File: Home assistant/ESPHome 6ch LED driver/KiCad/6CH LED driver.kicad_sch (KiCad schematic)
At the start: 75 parts, among them J1 DC Power, J10 I2C ext, J11 UART int, J12 UART ext, J13 IO Out, J14 U Out, J2 USB_C_small, J3 LED 1, J4 LED 2, J5 LED 3, J6 LED 4, J7 LED 5, J8 LED 6, J9 I2C int, Q1 AP4409AGEM, Q2 AP4409AGEM, Q3 AO3400A, Q4 AO3400A, Q5 AO3400A, Q6 AO3400A, Q7 AO3400A, Q8 AO3400A, SW1 Reset, SW2 Boot, U1 TPS5430DDA, U2 AMS1117-3.3, U3 ESP32-C6-WROOM-1

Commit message: Fix USB
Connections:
- net USB D+: now also R4.1; no longer R5.1
- net USB D-: now also R5.1; no longer R4.1
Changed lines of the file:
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@@
-    )
-  )
-  (global_label "USB D+" (shape bidirectional) (at 114.3 36.83 0) (fields_autoplaced)
-    (effects (font (size 1 1)) (justify left))
-    (property "Intersheetrefs" "${INTERSHEET_REFS}" (at 123.5253 36.83 0)
-      (effects (font (size 1.27 1.27)) (justify left) hide)
     )
   )
@@
     )
   )
+  (global_label "USB D+" (shape bidirectional) (at 114.3 31.75 0) (fields_autoplaced)
+    (effects (font (size 1 1)) (justify left))
+    (property "Intersheetrefs" "${INTERSHEET_REFS}" (at 123.5253 31.75 0)
+      (effects (font (size 1.27 1.27)) (justify left) hide)
+    )
+  )
   (global_label "RX" (shape bidirectional) (at 266.7 113.03 180) (fields_autoplaced)
     (effects (font (size 1.27 1.27)) (justify right))
     (property "Intersheetrefs" "${INTERSHEET_REFS}" (at 260.124 113.03 0)
       (effects (font (size 1.27 1.27)) (justify right) hide)
+    )
+  )
+  (global_label "USB D-" (shape bidirectional) (at 114.3 36.83 0) (fields_autoplaced)
+    (effects (font (size 1 1)) (justify left))
+    (property "Intersheetrefs" "${INTERSHEET_REFS}" (at 123.5253 36.83 0)
+      (effects (font (size 1.27 1.27)) (justify left) hide)
     )
   )
@@
     )
   )
-  (global_label "USB D-" (shape bidirectional) (at 114.3 31.75 0) (fields_autoplaced)
-    (effects (font (size 1 1)) (justify left))
-    (property "Intersheetrefs" "${INTERSHEET_REFS}" (at 123.5253 31.75 0)
-      (effects (font (size 1.27 1.27)) (justify left) hide)
-    )
-  )

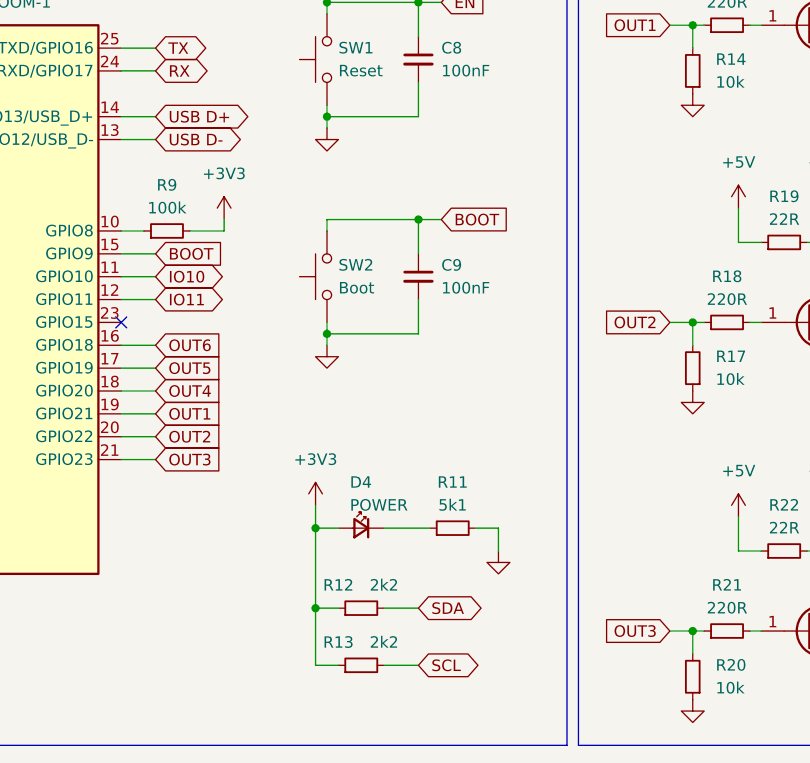
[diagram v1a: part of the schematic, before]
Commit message: Fix boot mode
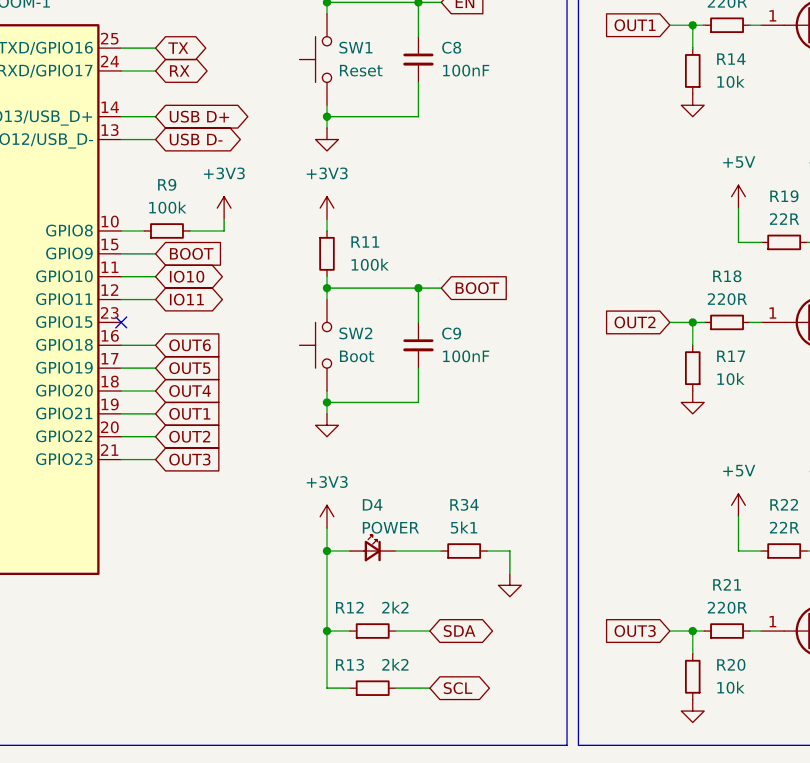
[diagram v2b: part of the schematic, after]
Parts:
- added R11: 100k, Resistor_SMD:R_0603_1608Metric, symbol Device:R_Small
- renumbered R11 to R34
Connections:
- net +3V3: now also R11.1
- net BOOT: now also R11.2
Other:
- moved on the sheet: C9, D4, R12, R13, R34, SW2
